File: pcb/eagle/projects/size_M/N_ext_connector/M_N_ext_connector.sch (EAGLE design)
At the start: 16 parts

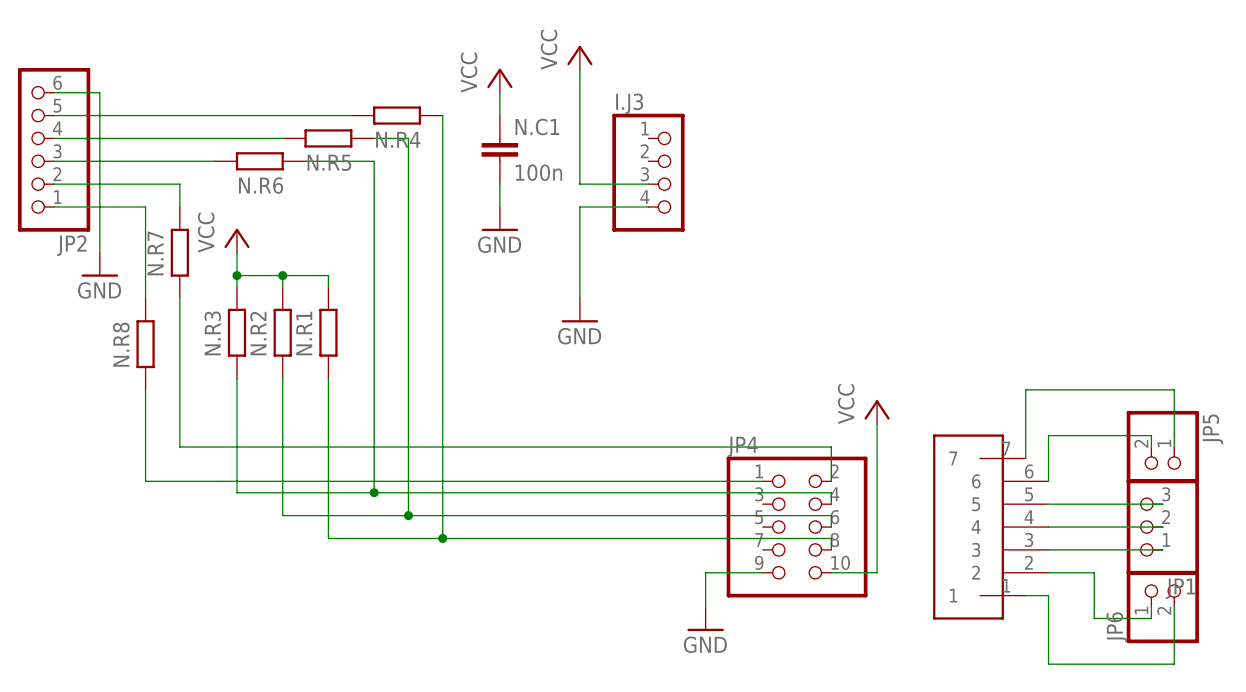
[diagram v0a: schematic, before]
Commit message: not finished meteo block
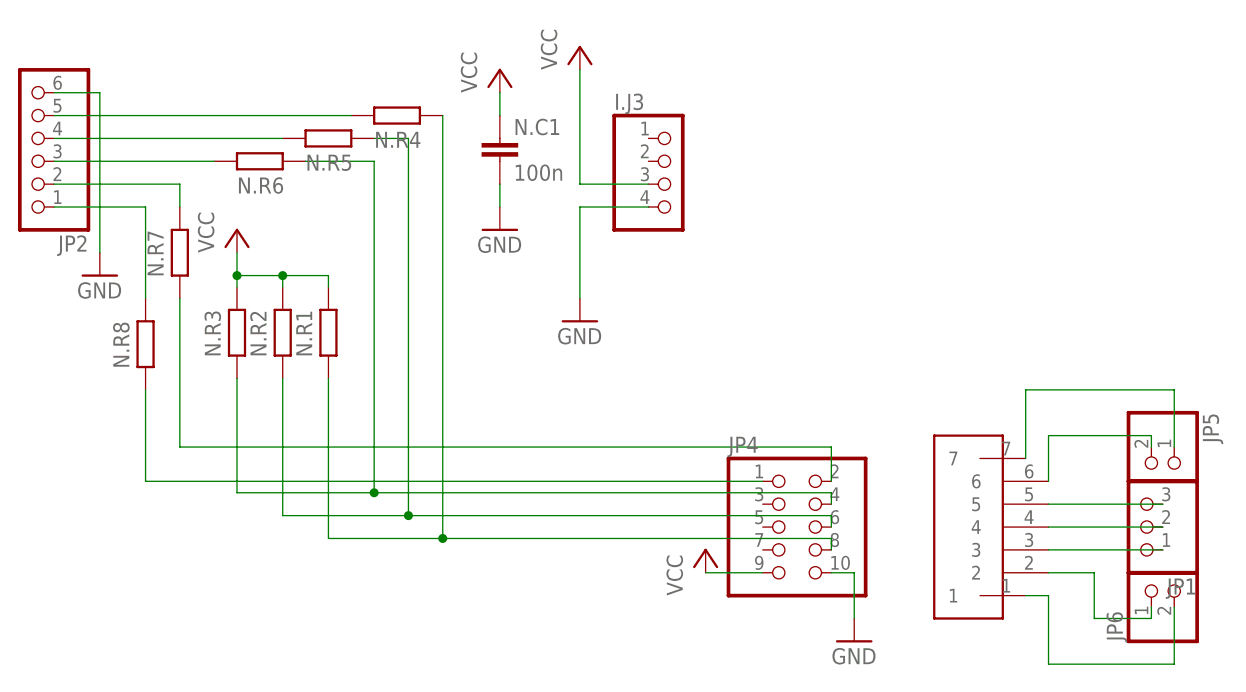
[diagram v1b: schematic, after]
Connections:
- net GND: now also JP4.10; no longer JP4.9
- net GND1: now also JP5.2, U$1.6; no longer JP5.1, U$1.7
- net VCC: now also JP4.9; no longer JP4.10
- net VCC1: now also JP5.1, U$1.7; no longer JP5.2, U$1.6
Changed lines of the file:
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@@
 <attribute name="VALUE" x="111.76" y="20.32" size="1.778" layer="96"/>
 </instance>
-<instance part="GND4" gate="1" x="128.27" y="-11.43" smashed="yes">
-<attribute name="VALUE" x="125.73" y="-13.97" size="1.778" layer="96"/>
+<instance part="GND4" gate="1" x="144.78" y="-12.7" smashed="yes">
+<attribute name="VALUE" x="142.24" y="-15.24" size="1.778" layer="96"/>
 </instance>
 <instance part="GND5" gate="1" x="60.96" y="27.94" smashed="yes">
 <attribute name="VALUE" x="58.42" y="25.4" size="1.778" layer="96"/>
 </instance>
-<instance part="P+4" gate="VCC" x="147.32" y="13.97" smashed="yes">
-<attribute name="VALUE" x="144.78" y="11.43" size="1.778" layer="96" rot="R90"/>
+<instance part="P+4" gate="VCC" x="128.27" y="-2.54" smashed="yes">
+<attribute name="VALUE" x="125.73" y="-7.62" size="1.778" layer="96" rot="R90"/>
 </instance>
 <instance part="P+3" gate="VCC" x="76.2" y="33.02" smashed="yes">
@@
 </segment>
 <segment>
-<pinref part="JP4" gate="A" pin="9"/>
 <pinref part="GND4" gate="1" pin="GND"/>
-<wire x1="134.62" y1="-5.08" x2="128.27" y2="-5.08" width="0.1524" layer="91"/>
-<wire x1="128.27" y1="-5.08" x2="128.27" y2="-8.89" width="0.1524" layer="91"/>
+<wire x1="142.24" y1="-5.08" x2="144.78" y2="-5.08" width="0.1524" layer="91"/>
+<wire x1="144.78" y1="-5.08" x2="144.78" y2="-10.16" width="0.1524" layer="91"/>
+<pinref part="JP4" gate="A" pin="10"/>
 </segment>
 </net>
@@
 <segment>
 <pinref part="P+4" gate="VCC" pin="VCC"/>
-<pinref part="JP4" gate="A" pin="10"/>
-<wire x1="147.32" y1="11.43" x2="147.32" y2="-5.08" width="0.1524" layer="91"/>
-<wire x1="147.32" y1="-5.08" x2="142.24" y2="-5.08" width="0.1524" layer="91"/>
+<wire x1="128.27" y1="-5.08" x2="134.62" y2="-5.08" width="0.1524" layer="91"/>
+<pinref part="JP4" gate="A" pin="9"/>
 </segment>
 </net>
@@
 </segment>
 </net>
-<net name="VCC1" class="0">
+<net name="GND1" class="0">
 <segment>
 <pinref part="U$1" gate="G$1" pin="6"/>
@@
 </segment>
 </net>
-<net name="GND1" class="0">
+<net name="VCC1" class="0">
 <segment>
 <pinref part="U$1" gate="G$1" pin="7"/>

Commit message: just adjustments
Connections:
- net N$1 renamed PA6
- net N$12 renamed PA7
- net N$13 renamed SDA1
- net N$14 renamed PA3
- removed net N$15: JP6.2, U$1.1
- new net SCL1: JP5.2, U$1.6
- net GND: now also JP4.1; no longer JP4.10
- net GND1: now also JP5.1, U$1.7; no longer JP5.2, U$1.6
- net N$10: now also JP4.4; no longer JP4.2
- net N$11: now also JP4.2; no longer JP4.1
- net N$2: now also JP4.10; no longer JP4.8
- net N$3: now also JP4.8; no longer JP4.6
- net N$9: now also JP4.6; no longer JP4.4
- net VCC1: now also JP6.2, U$1.1; no longer JP5.1, U$1.7
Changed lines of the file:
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@@
 <attribute name="VALUE" x="111.76" y="20.32" size="1.778" layer="96"/>
 </instance>
-<instance part="GND4" gate="1" x="144.78" y="-12.7" smashed="yes">
-<attribute name="VALUE" x="142.24" y="-15.24" size="1.778" layer="96"/>
+<instance part="GND4" gate="1" x="119.38" y="-7.62" smashed="yes">
+<attribute name="VALUE" x="116.84" y="-10.16" size="1.778" layer="96"/>
 </instance>
 <instance part="GND5" gate="1" x="60.96" y="27.94" smashed="yes">
 <attribute name="VALUE" x="58.42" y="25.4" size="1.778" layer="96"/>
 </instance>
-<instance part="P+4" gate="VCC" x="128.27" y="-2.54" smashed="yes">
-<attribute name="VALUE" x="125.73" y="-7.62" size="1.778" layer="96" rot="R90"/>
+<instance part="P+4" gate="VCC" x="125.73" y="15.24" smashed="yes">
+<attribute name="VALUE" x="123.19" y="10.16" size="1.778" layer="96" rot="R90"/>
 </instance>
 <instance part="P+3" gate="VCC" x="76.2" y="33.02" smashed="yes">
@@
 <segment>
 <pinref part="GND4" gate="1" pin="GND"/>
-<wire x1="142.24" y1="-5.08" x2="144.78" y2="-5.08" width="0.1524" layer="91"/>
-<wire x1="144.78" y1="-5.08" x2="144.78" y2="-10.16" width="0.1524" layer="91"/>
-<pinref part="JP4" gate="A" pin="10"/>
+<pinref part="JP4" gate="A" pin="1"/>
+<wire x1="119.38" y1="-5.08" x2="119.38" y2="5.08" width="0.1524" layer="91"/>
+<wire x1="119.38" y1="5.08" x2="134.62" y2="5.08" width="0.1524" layer="91"/>
 </segment>
 </net>
@@
 <segment>
 <pinref part="P+4" gate="VCC" pin="VCC"/>
-<wire x1="128.27" y1="-5.08" x2="134.62" y2="-5.08" width="0.1524" layer="91"/>
 <pinref part="JP4" gate="A" pin="9"/>
+<wire x1="125.73" y1="12.7" x2="125.73" y2="-5.08" width="0.1524" layer="91"/>
+<wire x1="125.73" y1="-5.08" x2="134.62" y2="-5.08" width="0.1524" layer="91"/>
 </segment>
 </net>
 <net name="N$2" class="0">
 <segment>
-<wire x1="86.36" y1="-1.27" x2="99.06" y2="-1.27" width="0.1524" layer="91"/>
+<wire x1="86.36" y1="-3.81" x2="99.06" y2="-3.81" width="0.1524" layer="91"/>
 <pinref part="N.R1" gate="G$1" pin="2"/>
-<wire x1="86.36" y1="16.51" x2="86.36" y2="-1.27" width="0.1524" layer="91"/>
-<wire x1="99.06" y1="-1.27" x2="99.06" y2="45.72" width="0.1524" layer="91"/>
+<wire x1="86.36" y1="16.51" x2="86.36" y2="-3.81" width="0.1524" layer="91"/>
+<wire x1="99.06" y1="-3.81" x2="99.06" y2="45.72" width="0.1524" layer="91"/>
 <pinref part="N.R4" gate="G$1" pin="2"/>
+<wire x1="99.06" y1="-3.81" x2="142.24" y2="-3.81" width="0.1524" layer="91"/>
+<junction x="99.06" y="-3.81"/>
+<pinref part="JP4" gate="A" pin="10"/>
+<wire x1="142.24" y1="-5.08" x2="142.24" y2="-3.81" width="0.1524" layer="91"/>
+</segment>
+</net>
+<net name="N$3" class="0">
+<segment>
+<wire x1="81.28" y1="-1.27" x2="95.25" y2="-1.27" width="0.1524" layer="91"/>
+<pinref part="N.R2" gate="G$1" pin="2"/>
+<wire x1="81.28" y1="16.51" x2="81.28" y2="-1.27" width="0.1524" layer="91"/>
+<wire x1="91.44" y1="43.18" x2="95.25" y2="43.18" width="0.1524" layer="91"/>
+<wire x1="95.25" y1="43.18" x2="95.25" y2="-1.27" width="0.1524" layer="91"/>
+<pinref part="N.R5" gate="G$1" pin="2"/>
+<wire x1="95.25" y1="-1.27" x2="142.24" y2="-1.27" width="0.1524" layer="91"/>
+<junction x="95.25" y="-1.27"/>
 <pinref part="JP4" gate="A" pin="8"/>
-<wire x1="99.06" y1="-1.27" x2="142.24" y2="-1.27" width="0.1524" layer="91"/>
-<wire x1="142.24" y1="-1.27" x2="142.24" y2="-2.54" width="0.1524" layer="91"/>
-<junction x="99.06" y="-1.27"/>
-</segment>
-</net>
-<net name="N$3" class="0">
-<segment>
-<wire x1="81.28" y1="1.27" x2="95.25" y2="1.27" width="0.1524" layer="91"/>
-<pinref part="N.R2" gate="G$1" pin="2"/>
-<wire x1="81.28" y1="16.51" x2="81.28" y2="1.27" width="0.1524" layer="91"/>
-<wire x1="91.44" y1="43.18" x2="95.25" y2="43.18" width="0.1524" layer="91"/>
-<wire x1="95.25" y1="43.18" x2="95.25" y2="1.27" width="0.1524" layer="91"/>
-<pinref part="N.R5" gate="G$1" pin="2"/>
-<pinref part="JP4" gate="A" pin="6"/>
-<wire x1="95.25" y1="1.27" x2="142.24" y2="1.27" width="0.1524" layer="91"/>
-<wire x1="142.24" y1="1.27" x2="142.24" y2="0" width="0.1524" layer="91"/>
-<junction x="95.25" y="1.27"/>
+<wire x1="142.24" y1="-2.54" x2="142.24" y2="-1.27" width="0.1524" layer="91"/>
 </segment>
 </net>
 <net name="N$10" class="0">
 <segment>
-<wire x1="69.85" y1="25.4" x2="69.85" y2="8.89" width="0.1524" layer="91"/>
+<wire x1="69.85" y1="25.4" x2="69.85" y2="3.81" width="0.1524" layer="91"/>
 <pinref part="N.R7" gate="G$1" pin="2"/>
-<pinref part="JP4" gate="A" pin="2"/>
-<wire x1="142.24" y1="5.08" x2="142.24" y2="8.89" width="0.1524" layer="91"/>
-<wire x1="142.24" y1="8.89" x2="69.85" y2="8.89" width="0.1524" layer="91"/>
+<wire x1="143.51" y1="3.81" x2="69.85" y2="3.81" width="0.1524" layer="91"/>
+<pinref part="JP4" gate="A" pin="4"/>
+<wire x1="142.24" y1="2.54" x2="143.51" y2="2.54" width="0.1524" layer="91"/>
+<wire x1="143.51" y1="2.54" x2="143.51" y2="3.81" width="0.1524" layer="91"/>
 </segment>
 </net>
@@
 <net name="N$11" class="0">
 <segment>
-<pinref part="JP4" gate="A" pin="1"/>
-<wire x1="66.04" y1="15.24" x2="66.04" y2="5.08" width="0.1524" layer="91"/>
 <pinref part="N.R8" gate="G$1" pin="2"/>
-<wire x1="134.62" y1="5.08" x2="66.04" y2="5.08" width="0.1524" layer="91"/>
+<wire x1="66.04" y1="15.24" x2="66.04" y2="6.35" width="0.1524" layer="91"/>
+<pinref part="JP4" gate="A" pin="2"/>
+<wire x1="142.24" y1="5.08" x2="142.24" y2="6.35" width="0.1524" layer="91"/>
+<wire x1="142.24" y1="6.35" x2="66.04" y2="6.35" width="0.1524" layer="91"/>
 </segment>
 </net>
 <net name="N$9" class="0">
 <segment>
-<pinref part="JP4" gate="A" pin="4"/>
-<wire x1="142.24" y1="2.54" x2="142.24" y2="3.81" width="0.1524" layer="91"/>
-<wire x1="76.2" y1="3.81" x2="91.44" y2="3.81" width="0.1524" layer="91"/>
+<wire x1="76.2" y1="1.27" x2="91.44" y2="1.27" width="0.1524" layer="91"/>
 <pinref part="N.R3" gate="G$1" pin="2"/>
-<wire x1="76.2" y1="16.51" x2="76.2" y2="3.81" width="0.1524" layer="91"/>
+<wire x1="76.2" y1="16.51" x2="76.2" y2="1.27" width="0.1524" layer="91"/>
 <wire x1="83.82" y1="40.64" x2="91.44" y2="40.64" width="0.1524" layer="91"/>
-<wire x1="91.44" y1="40.64" x2="91.44" y2="3.81" width="0.1524" layer="91"/>
+<wire x1="91.44" y1="40.64" x2="91.44" y2="1.27" width="0.1524" layer="91"/>
 <pinref part="N.R6" gate="G$1" pin="2"/>
-<wire x1="142.24" y1="3.81" x2="91.44" y2="3.81" width="0.1524" layer="91"/>
-<junction x="91.44" y="3.81"/>
-</segment>
-</net>
-<net name="N$14" class="0">
+<wire x1="142.24" y1="1.27" x2="91.44" y2="1.27" width="0.1524" layer="91"/>
+<junction x="91.44" y="1.27"/>
+<pinref part="JP4" gate="A" pin="6"/>
+<wire x1="142.24" y1="0" x2="142.24" y2="1.27" width="0.1524" layer="91"/>
+</segment>
+</net>
+<net name="PA3" class="0">
 <segment>
 <pinref part="U$1" gate="G$1" pin="2"/>
@@
 </segment>
 </net>
-<net name="N$15" class="0">
+<net name="VCC1" class="0">
 <segment>
 <pinref part="U$1" gate="G$1" pin="1"/>
@@
 </segment>
 </net>
-<net name="N$12" class="0">
+<net name="PA7" class="0">
 <segment>
 <pinref part="U$1" gate="G$1" pin="4"/>
@@
 </segment>
 </net>
-<net name="N$13" class="0">
+<net name="SDA1" class="0">
 <segment>
 <pinref part="JP1" gate="A" pin="3"/>
@@
 </segment>
 </net>
-<net name="GND1" class="0">
+<net name="SCL1" class="0">
 <segment>
 <pinref part="U$1" gate="G$1" pin="6"/>
@@
 </segment>
 </net>
-<net name="VCC1" class="0">
+<net name="GND1" class="0">
 <segment>
 <pinref part="U$1" gate="G$1" pin="7"/>
@@
 </segment>
 </net>
-<net name="N$1" class="0">
+<net name="PA6" class="0">
 <segment>
 <pinref part="U$1" gate="G$1" pin="3"/>

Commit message: PCB v7 * 14 pin attiny is main adapter chip now. * changed adapter pin meaning (a1-a5, swapped RX-TX, VUSB replaced by A5, top most pin changed from GND to A4) * changed usb chip of main board
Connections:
- net GND: no longer JP2.6
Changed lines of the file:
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@@
 <setting verticaltext="up"/>
 </settings>
-<grid distance="0.05" unitdist="inch" unit="inch" style="lines" multiple="1" display="no" altdistance="0.01" altunitdist="inch" altunit="inch"/>
+<grid distance="0.1" unitdist="inch" unit="inch" style="lines" multiple="1" display="no" altdistance="0.01" altunitdist="inch" altunit="inch"/>
 <layers>
 <layer number="1" name="Top" color="4" fill="1" visible="no" active="no"/>
@@
 <part name="GND3" library="supply1" library_urn="urn:adsk.eagle:library:371" deviceset="GND" device=""/>
 <part name="GND4" library="supply1" library_urn="urn:adsk.eagle:library:371" deviceset="GND" device=""/>
-<part name="GND5" library="supply1" library_urn="urn:adsk.eagle:library:371" deviceset="GND" device=""/>
 <part name="P+4" library="supply1" library_urn="urn:adsk.eagle:library:371" deviceset="VCC" device=""/>
 <part name="P+3" library="supply1" library_urn="urn:adsk.eagle:library:371" deviceset="VCC" device=""/>
@@
 <attribute name="VALUE" x="116.84" y="-10.16" size="1.778" layer="96"/>
 </instance>
-<instance part="GND5" gate="1" x="60.96" y="27.94" smashed="yes">
-<attribute name="VALUE" x="58.42" y="25.4" size="1.778" layer="96"/>
-</instance>
 <instance part="P+4" gate="VCC" x="125.73" y="15.24" smashed="yes">
 <attribute name="VALUE" x="123.19" y="10.16" size="1.778" layer="96" rot="R90"/>
@@
 </segment>
 <segment>
-<pinref part="JP2" gate="A" pin="6"/>
-<wire x1="60.96" y1="48.26" x2="55.88" y2="48.26" width="0.1524" layer="91"/>
-<pinref part="GND5" gate="1" pin="GND"/>
-<wire x1="60.96" y1="30.48" x2="60.96" y2="48.26" width="0.1524" layer="91"/>
-</segment>
-<segment>
